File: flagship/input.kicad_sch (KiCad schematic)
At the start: 10 parts, among them J1 BUS_IN, Q1 HOTSWAP_FET, Q2 IDEAL_DIODE_FET, U1 LTC4364IS-2

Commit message: flagship: input protection latches off (LTC4364-1) with a raw-input-powered fault LED; candidate ICs accepted (SPEC rulings)
Co-Authored-By: Claude Opus 5.5 (1M context) <noreply@anthropic.com>
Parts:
- added D6: RED_FAULT, LED_SMD:LED_1206_3216Metric, symbol Device:LED
- added R30: 18k, Resistor_SMD:R_1206_3216Metric, symbol Device:R
- U1: value LTC4364IS-2 -> LTC4364IS-1
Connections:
- net VIN_RAW: now also R30.1
- net LTC_FLT_N: now reaches U1.13 (~{FLT})
- net LTC_FLT_N: now also D6.1 (K)
- new net FLT_LED_A: D6.2 (A), R30.2
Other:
- note added: "INPUT PROTECTION (record section 3). Self-acting: nothing here depends on firmware or on a rail it protects. Jobs: reverse polarity, reverse-current blocking (required so the regen clamp can sit at ~45 V, section 5), inrush, overcurrent. U1 LTC4364IS-1 (SO-16): surge stopper + ideal diode in one part. LATCH-OFF (-1, operator ruling 2026-09-22): a fault kills every rail, MCU included, so D6 is pow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"
- note removed: "INPUT PROTECTION (record section 3). Self-acting: nothing here depends on firmware or on a rail it protects. Jobs: reverse polarity, reverse-current blocking (required so the regen clamp can sit at ~45 V, section 5), inrush, overcurrent. Candidate U1 LTC4364IS-2 (SO-16): surge stopper + ideal diode in one part. -2 = auto-retry after fault, -1 = latch off: ruling needed. TODO(detailing): wire Q1/Q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"
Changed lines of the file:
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@@
 	(generator_version "10.0")
 	(paper "A4")
-	(text "INPUT PROTECTION (record section 3). Self-acting: nothing here depends on firmware or on a rail it protects.\nJobs: reverse polarity, reverse-current blocking (required so the regen clamp can sit at ~45 V, section 5), inrush, overcurrent.\nCandidate U1 LTC4364IS-2 (SO-16): surge stopper + ideal diode in one part. -2 = auto-retry after fault, -1 = latch off: ruling needed.\nTODO(detailing): wire Q1/Q2/R1 per LTC4364 datasheet Figure 1; Q1 chosen off its pulse SOA curve (1000 uF at 36 V = ~0.65 J in linear region).\nR2 is the INA228 shunt: Kelvin taps INA_SENSE_P (BUS_PROT side) and INA_SENSE_N (+BUS side) route as a tight pair to the Sensing sheet.\nBulk: C1/C2 polymer mirrored about the stamp centerline (SPEC ruling), C3/C4 MLCC for HF. Decoupling only; caps do nothing for regen."
+	(text "INPUT PROTECTION (record section 3). Self-acting: nothing here depends on firmware or on a rail it protects.\nJobs: reverse polarity, reverse-current blocking (required so the regen clamp can sit at ~45 V, section 5), inrush, overcurrent.\nU1 LTC4364IS-1 (SO-16): surge stopper + ideal diode in one part. LATCH-OFF (-1, operator ruling 2026-09-22): a fault kills every rail, MCU included,\nso D6 is powered from VIN_RAW and lit by FLT: the fault shows with the board dark. Power-cycle clears it. TODO(detailing): confirm FLT pin's voltage rating vs VIN.\nTODO(detailing): wire Q1/Q2/R1 per LTC4364 datasheet Figure 1; Q1 chosen off its pulse SOA curve (1000 uF at 36 V = ~0.65 J in linear region).\nR2 is the INA228 shunt: Kelvin taps INA_SENSE_P (BUS_PROT side) and INA_SENSE_N (+BUS side) route as a tight pair to the Sensing sheet.\nBulk: C1/C2 polymer mirrored about the stamp centerline (SPEC ruling), C3/C4 MLCC for HF. Decoupling only; caps do nothing for regen."
 		(exclude_from_sim no)
 		(at 20 150 0)
@@
 		)
 	)
+	(wire
+		(pts
+			(xy 59.69 125.73) (xy 59.69 114.3)
+		)
+		(stroke
+			(width 0)
+			(type default)
+		)
+	)
 	(label "VIN_RAW"
 		(at 25.4 80.01 180)
@@
 		)
 	)
+	(label "FLT_LED_A"
+		(at 59.69 114.3 270)
+		(effects
+			(font
+				(size 1.27 1.27)
+			)
+			(justify right bottom)
+		)
+	)
+	(label "LTC_FLT_N"
+		(at 59.69 133.35 270)
+		(effects
+			(font
+				(size 1.27 1.27)
+			)
+			(justify right bottom)
+		)
+	)
 	(label "BUS_PROT"
 		(at 170.18 69.85 90)
@@
 			)
 			(justify right bottom)
+		)
+	)
+	(label "VIN_RAW"
+		(at 59.69 106.68 90)
+		(effects
+			(font
+				(size 1.27 1.27)
+			)
+			(justify left bottom)
+		)
+	)
+	(label "LTC_FLT_N"
+		(at 124.46 109.22 0)
+		(effects
+			(font
+				(size 1.27 1.27)
+			)
+			(justify left bottom)
 		)
 	)
@@
 	)
 	(symbol
+		(lib_id "Device:R")
+		(at 59.69 110.49 0)
+		(unit 1)
+		(body_style 1)
+		(exclude_from_sim no)
+		(in_bom yes)
+		(on_board yes)
+		(in_pos_files yes)
+		(dnp no)
+		(property "Reference" "R30"
+			(at 57.15 110.49 0)
+			(show_name no)
+			(do_not_autoplace no)
+			(effects
+				(font
+					(size 1.27 1.27)
+				)
+			)
+		)
+		(property "Value" "18k"
+			(at 62.23 110.49 0)
+			(show_name no)
+			(do_not_autoplace no)
+			(effects
+				(font
+					(size 1.27 1.27)
+				)
+			)
+		)
+		(property "Footprint" "Resistor_SMD:R_1206_3216Metric"
+			(at 57.912 110.49 90)
+			(hide yes)
+			(show_name no)
+			(do_not_autoplace no)
+			(effects
+				(font
+					(size 1.27 1.27)
+				)
+			)
+		)
+		(property "Datasheet" ""
+			(at 59.69 110.49 0)
+			(hide yes)
+			(show_name no)
+			(do_not_autoplace no)
+			(effects
+				(font
+					(size 1.27 1.27)
+				)
+			)
+		)
+		(property "Description" "Resistor"
+			(at 59.69 110.49 0)
+			(hide yes)
+			(show_name no)
+			(do_not_autoplace no)
+			(effects
+				(font
+					(size 1.27 1.27)
+				)
+			)
+		)
+		(pin "1"
+		)
+		(pin "2"
+		)
+		(instances
+			(project ""
+				(path "/8c22eeb1-303f-4db8-b0be-7d6b88218484"
+					(reference "R30")
+					(unit 1)
+				)
+			)
+		)
+	)
+	(symbol
 		(lib_id "Device:Q_NMOS")
 		(at 80.01 69.85 0)
@@
 			)
 		)
-		(property "Value" "LTC4364IS-2"
+		(property "Value" "LTC4364IS-1"
 			(at 110.49 97.79 0)
 			(show_name no)
@@
 					(unit 1)
 				)
+			)
+		)
+	)
+	(symbol
+		(lib_id "Device:LED")
+		(at 59.69 129.54 90)
+		(unit 1)
+		(body_style 1)
+		(exclude_from_sim no)
+		(in_bom yes)
+		(on_board yes)
+		(in_pos_files yes)
+		(dnp no)
+		(property "Reference" "D6"
+			(at 59.69 127 0)
+			(show_name no)
+			(do_not_autoplace no)
+			(effects
+				(font
+					(size 1.27 1.27)
+				)
+			)
+		)
+		(property "Value" "RED_FAULT"
+			(at 59.69 132.08 0)
+			(show_name no)
+			(do_not_autoplace no)
+			(effects
+				(font
+					(size 1.27 1.27)
+				)
+			)
+		)
+		(property "Footprint" "LED_SMD:LED_1206_3216Metric"
+			(at 59.69 129.54 0)
+			(hide yes)
+			(show_name no)
+			(do_not_autoplace no)
+			(effects
+				(font
+					(size 1.27 1.27)
+				)
+			)
+		)
+		(property "Datasheet" ""
+			(at 59.69 129.54 0)
+			(hide yes)
+			(show_name no)
+			(do_not_autoplace no)
+			(effects
+				(font
+					(size 1.27 1.27)
+				)
+			)
+		)
+		(property "Description" "Light emitting diode"
+			(at 59.69 129.54 0)
+			(hide yes)
+			(show_name no)
+			(do_not_autoplace no)
+			(effects
+				(font
+					(size 1.27 1.27)
+				)
+			)
+		)
+		(pin "1"
+		)
+		(pin "2"
+		)
+		(instances
+			(project ""
+				(path "/8c22eeb1-303f-4db8-b0be-7d6b88218484"
+					(reference "D6")
+					(unit 1)
+				)

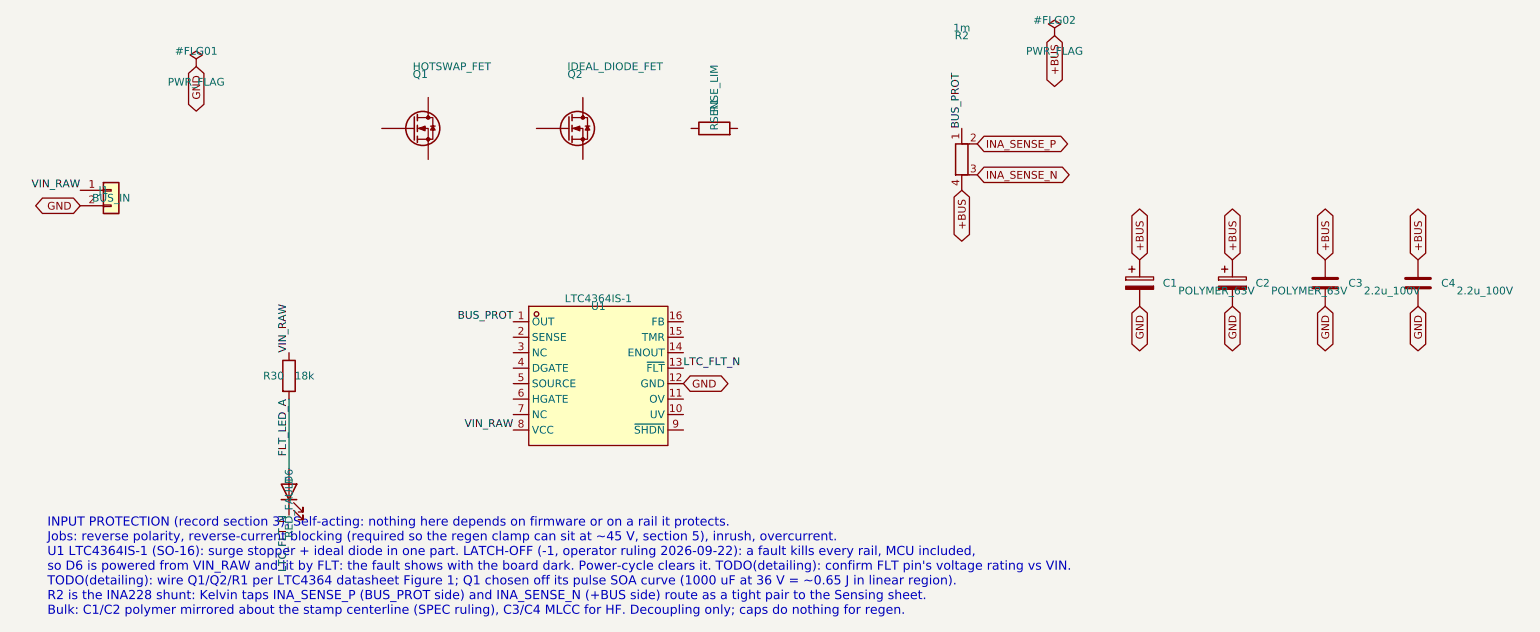
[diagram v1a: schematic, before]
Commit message: flagship: input fuse F1 (OMNI-BLOK 154 + Nano2 453 15 A, 65 V DC) first in the path; no polyfuse (SPEC ruling)
Co-Authored-By: Claude Opus 5.5 (1M context) <noreply@anthropic.com>
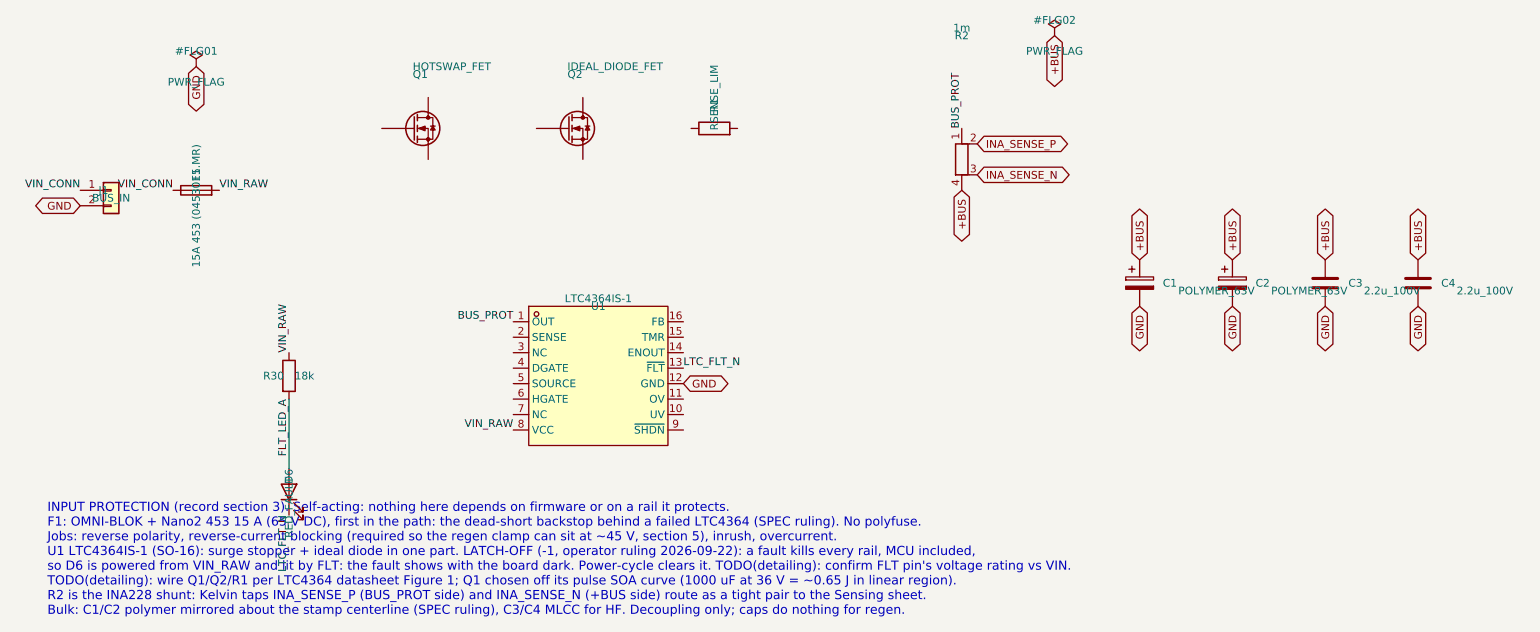
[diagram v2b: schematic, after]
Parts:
- added F1: 15A 453 (0453015.MR), Fuse:Fuseholder_Littelfuse_Nano2_154x, symbol Device:Fuse
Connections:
- net VIN_RAW: now also F1.2; no longer J1.1 (Pin_1)
- new net VIN_CONN: F1.1, J1.1 (Pin_1)
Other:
- note added: "INPUT PROTECTION (record section 3). Self-acting: nothing here depends on firmware or on a rail it protects. F1: OMNI-BLOK + Nano2 453 15 A (65 V DC), first in the path: the dead-short backstop behind a failed LTC4364 (SPEC ruling). No polyfuse. Jobs: reverse polarity, reverse-current blocking (required so the regen clamp can sit at ~45 V, section 5), inrush, overcurrent. U1 LTC4364IS-1 (SO-16): 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"
- note removed: "INPUT PROTECTION (record section 3). Self-acting: nothing here depends on firmware or on a rail it protects. Jobs: reverse polarity, reverse-current blocking (required so the regen clamp can sit at ~45 V, section 5), inrush, overcurrent. U1 LTC4364IS-1 (SO-16): surge stopper + ideal diode in one part. LATCH-OFF (-1, operator ruling 2026-09-22): a fault kills every rail, MCU included, so D6 is pow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"
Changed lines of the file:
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@@
 	(generator_version "10.0")
 	(paper "A4")
-	(text "INPUT PROTECTION (record section 3). Self-acting: nothing here depends on firmware or on a rail it protects.\nJobs: reverse polarity, reverse-current blocking (required so the regen clamp can sit at ~45 V, section 5), inrush, overcurrent.\nU1 LTC4364IS-1 (SO-16): surge stopper + ideal diode in one part. LATCH-OFF (-1, operator ruling 2026-09-22): a fault kills every rail, MCU included,\nso D6 is powered from VIN_RAW and lit by FLT: the fault shows with the board dark. Power-cycle clears it. TODO(detailing): confirm FLT pin's voltage rating vs VIN.\nTODO(detailing): wire Q1/Q2/R1 per LTC4364 datasheet Figure 1; Q1 chosen off its pulse SOA curve (1000 uF at 36 V = ~0.65 J in linear region).\nR2 is the INA228 shunt: Kelvin taps INA_SENSE_P (BUS_PROT side) and INA_SENSE_N (+BUS side) route as a tight pair to the Sensing sheet.\nBulk: C1/C2 polymer mirrored about the stamp centerline (SPEC ruling), C3/C4 MLCC for HF. Decoupling only; caps do nothing for regen."
+	(text "INPUT PROTECTION (record section 3). Self-acting: nothing here depends on firmware or on a rail it protects.\nF1: OMNI-BLOK + Nano2 453 15 A (65 V DC), first in the path: the dead-short backstop behind a failed LTC4364 (SPEC ruling). No polyfuse.\nJobs: reverse polarity, reverse-current blocking (required so the regen clamp can sit at ~45 V, section 5), inrush, overcurrent.\nU1 LTC4364IS-1 (SO-16): surge stopper + ideal diode in one part. LATCH-OFF (-1, operator ruling 2026-09-22): a fault kills every rail, MCU included,\nso D6 is powered from VIN_RAW and lit by FLT: the fault shows with the board dark. Power-cycle clears it. TODO(detailing): confirm FLT pin's voltage rating vs VIN.\nTODO(detailing): wire Q1/Q2/R1 per LTC4364 datasheet Figure 1; Q1 chosen off its pulse SOA curve (1000 uF at 36 V = ~0.65 J in linear region).\nR2 is the INA228 shunt: Kelvin taps INA_SENSE_P (BUS_PROT side) and INA_SENSE_N (+BUS side) route as a tight pair to the Sensing sheet.\nBulk: C1/C2 polymer mirrored about the stamp centerline (SPEC ruling), C3/C4 MLCC for HF. Decoupling only; caps do nothing for regen."
 		(exclude_from_sim no)
 		(at 20 150 0)
@@
 		)
 	)
-	(label "VIN_RAW"
-		(at 25.4 80.01 180)
+	(label "VIN_CONN"
+		(at 40.64 80.01 180)
 		(effects
 			(font
@@
 			)
 			(justify left bottom)
+		)
+	)
+	(label "VIN_RAW"
+		(at 48.26 80.01 0)
+		(effects
+			(font
+				(size 1.27 1.27)
+			)
+			(justify left bottom)
+		)
+	)
+	(label "VIN_CONN"
+		(at 25.4 80.01 180)
+		(effects
+			(font
+				(size 1.27 1.27)
+			)
+			(justify right bottom)
 		)
 	)
@@
 					(unit 1)
 				)
+			)
+		)
+	)
+	(symbol
+		(lib_id "Device:Fuse")
+		(at 44.45 80.01 90)
+		(unit 1)
+		(body_style 1)
+		(exclude_from_sim no)
+		(in_bom yes)
+		(on_board yes)
+		(in_pos_files yes)
+		(dnp no)
+		(property "Reference" "F1"
+			(at 44.45 77.47 0)
+			(show_name no)
+			(do_not_autoplace no)
+			(effects
+				(font
+					(size 1.27 1.27)
+				)
+			)
+		)
+		(property "Value" "15A 453 (0453015.MR)"
+			(at 44.45 82.55 0)
+			(show_name no)
+			(do_not_autoplace no)
+			(effects
+				(font
+					(size 1.27 1.27)
+				)
+			)
+		)
+		(property "Footprint" "Fuse:Fuseholder_Littelfuse_Nano2_154x"
+			(at 44.45 81.788 90)
+			(hide yes)
+			(show_name no)
+			(do_not_autoplace no)
+			(effects
+				(font
+					(size 1.27 1.27)
+				)
+			)
+		)
+		(property "Datasheet" ""
+			(at 44.45 80.01 0)
+			(hide yes)
+			(show_name no)
+			(do_not_autoplace no)
+			(effects
+				(font
+					(size 1.27 1.27)
+				)
+			)
+		)
+		(property "Description" "Fuse"
+			(at 44.45 80.01 0)
+			(hide yes)
+			(show_name no)
+			(do_not_autoplace no)
+			(effects
+				(font
+					(size 1.27 1.27)
+				)
+			)
+		)
+		(pin "1"
+		)
+		(pin "2"
+		)
+		(instances
+			(project ""
+				(path "/8c22eeb1-303f-4db8-b0be-7d6b88218484"
+					(reference "F1")
+					(unit 1)
+				)
